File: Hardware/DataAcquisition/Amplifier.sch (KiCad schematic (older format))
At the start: 21 parts, among them Q6 Q_NJFET_DGS, Q7 Q_NJFET_DGS, U4 LM358, U5 Opamp_Dual_Generic

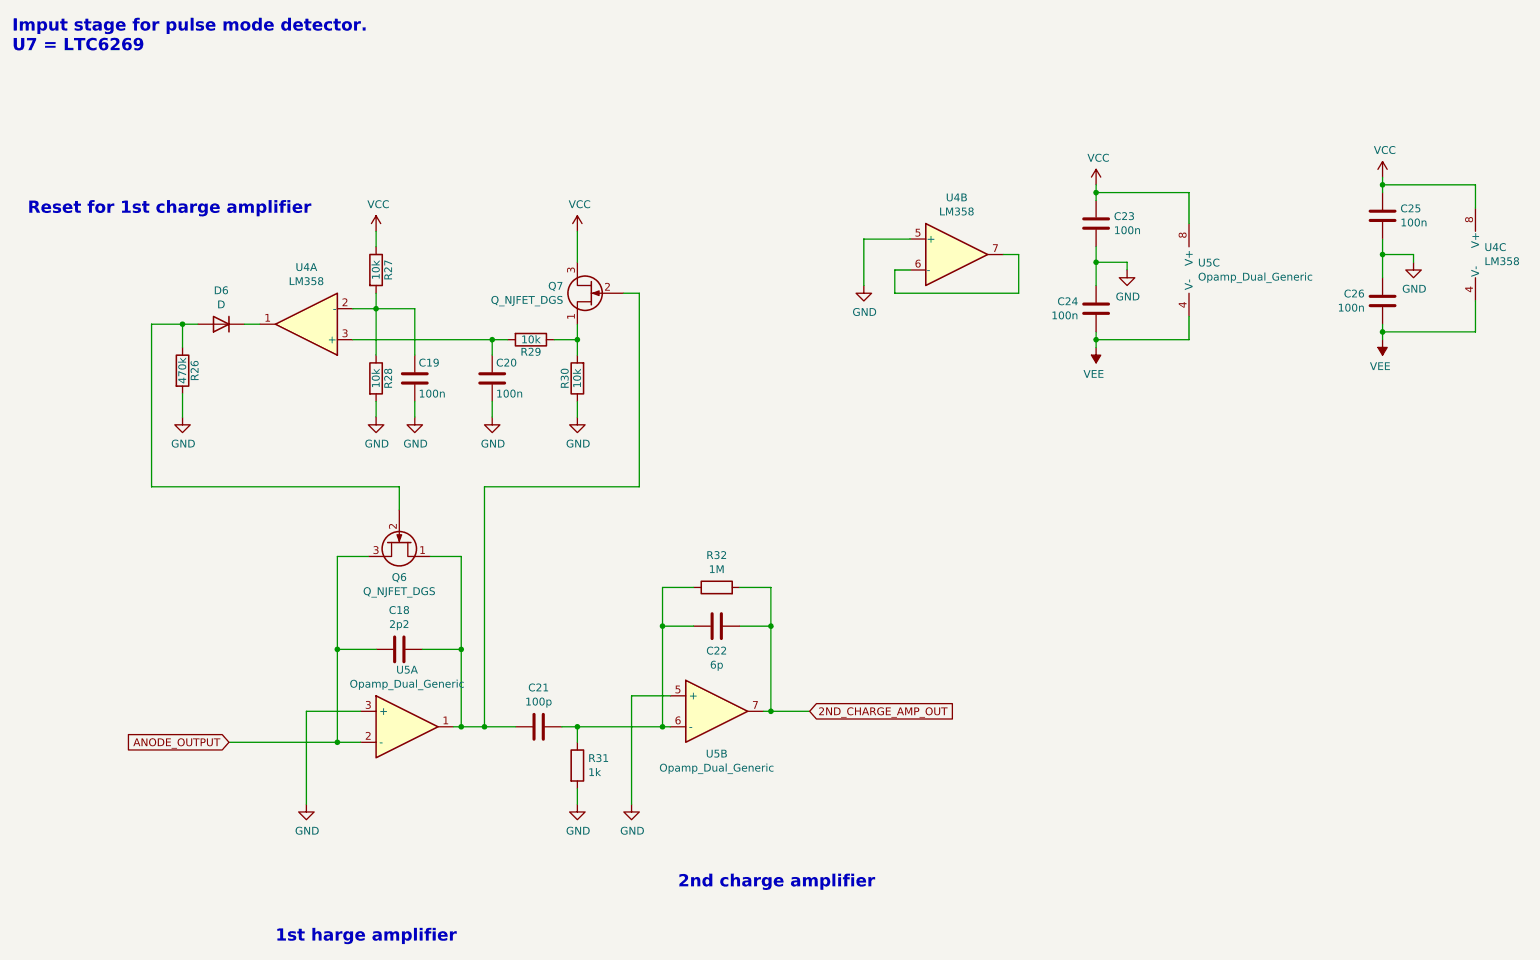
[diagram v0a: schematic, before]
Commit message: Clarify architecture of acquisition module (#80), removed obsolete files
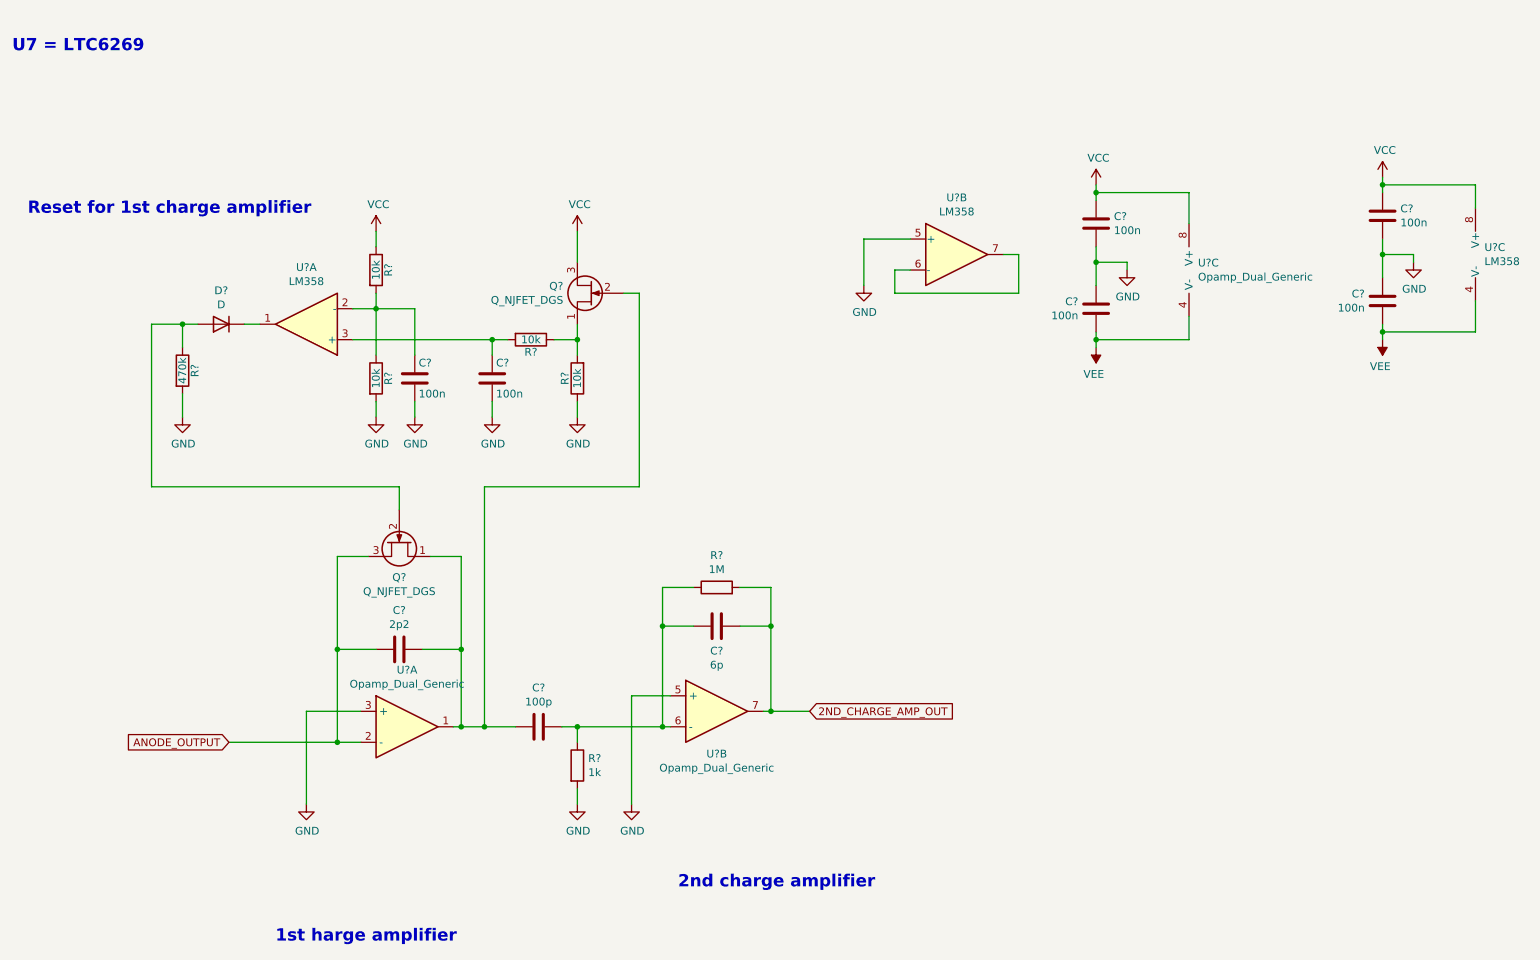
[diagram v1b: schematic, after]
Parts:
- renumbered D6 to D?, Q6 to Q?, Q7 to Q?, U5 to U?, U4 to U?
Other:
- note added: "U7 = LTC6269"
- note removed: "Imput stage for pulse mode detector.\nU7 = LTC6269"
